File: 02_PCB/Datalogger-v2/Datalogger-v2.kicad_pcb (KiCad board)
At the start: 2 copper layers, 140 x 90 mm, 21 parts, among them U1 Micro SD Card Adapter, U7 TP4056, U8 ESP32 DEV KIT DOIT

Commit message: Update PCB layout
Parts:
- added C4: 100uF/10V, Capacitor_THT:CP_Radial_D5.0mm_P2.50mm, F.Cu at (114.5, 88.0)
- added C5: 0.1uF_0603_16V, Capacitor_SMD:C_0805_2012Metric_Pad1.18x1.45mm_HandSolder, F.Cu at (103.0, 92.0)
- added R10: 4.7Ω, Resistor_THT:R_Axial_DIN0207_L6.3mm_D2.5mm_P10.16mm_Horizontal, F.Cu at (99.0, 112.0)
- added R11: 4.7Ω, Resistor_THT:R_Axial_DIN0207_L6.3mm_D2.5mm_P10.16mm_Horizontal, F.Cu at (107.0, 112.0)
- R1, R2, R3, R4: moved to B.Cu
- moved R2 38.3 mm to (120.7, 133.7)
- moved R1 32.8 mm to (128.7, 133.7)
- moved R5 21.6 mm to (153.1, 98.0), turned to 180 degrees
- moved R7 20.7 mm to (153.2, 86.0)
- moved R6 20.7 mm to (153.2, 92.0)
- moved D1 16.6 mm to (130.1, 88.0)
- moved R4 10.2 mm to (174.4, 79.0), turned to 180 degrees
- moved R8 10.2 mm to (161.4, 121.0), turned to 180 degrees
- moved R9 10.2 mm to (161.5, 115.0), turned to 180 degrees
- moved R3 10.2 mm to (174.3, 72.0), turned to 180 degrees
- moved U6 6.00 mm to (175.7, 112.1)
- moved C2 2.96 mm to (175.0, 127.0), turned to 90 degrees
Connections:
- C1 pad 1: GND -> +5V
- C1 pad 2: +5V -> GND
- U8 pad 10: Net-(U5-SDA) -> +5V
- U8 pad 11: Net-(U5-SCL) -> +5V
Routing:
- net +5V: track 157.5 -> 336.3 mm, vias 3 -> 11
- net GND: track 149.2 -> 236.1 mm, vias 2 -> 11
- net Net-(U4-TX): track 0.00 -> 78.1 mm, vias 0 -> 4
- net Net-(U6-RX): track 0.00 -> 75.4 mm, vias 0 -> 4
- net Net-(U4-RX): track 0.00 -> 71.1 mm, vias 0 -> 2
- net +3.3V: track 103.1 -> 60.2 mm
- net Net-(U8-ADC/D4): track 0.00 -> 36.4 mm, vias 0 -> 2
- net Net-(U5-SCL): track 69.9 -> 48.9 mm, vias 1 -> 0
- net Net-(U1-MOSI): track 15.8 -> 35.2 mm, vias 0 -> 3
- net Net-(U1-CS): track 0.00 -> 19.1 mm, vias 0 -> 1
- net Net-(U1-SCK): track 0.10 -> 18.7 mm, vias 0 -> 2
- net Net-(U5-SDA): track 65.8 -> 48.7 mm, vias 1 -> 0
- net Net-(U8-ADC/DAC1/D26): track 40.6 -> 53.9 mm, vias 1 -> 2
- net Net-(U8-ADC/DAC0/D25): track 41.8 -> 55.1 mm, vias 1 -> 2
- net Net-(U2-VIN+): track 66.2 -> 56.2 mm
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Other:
- board text added: "TO DOs: - Check and change vias size - Check and change trace width (with PCB calculator in KiCad. INTERNAL LAYER result)"
- board text added: "We <3 feet here"

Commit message: Update PCB schematic
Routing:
- net GND: track 236.1 -> 295.9 mm, vias 11 -> 15
- net Net-(U8-ADC/DAC0/D25): track 55.1 -> 56.2 mm
- net +5V: vias 11 -> 10

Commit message: Update schematics and PCB design
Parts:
- moved C5 2.00 mm to (103.0, 94.0)
- moved C3 0.65 mm to (76.0, 82.0), turned to 180 degrees
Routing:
- net Net-(U8-ADC/D13): track 93.5 -> 122.8 mm
- net GND: track 295.9 -> 287.5 mm, vias 15 -> 11
- net +5V: track 336.3 -> 334.5 mm, vias 10 -> 9
- net Net-(U8-ADC/DAC0/D25): track 56.2 -> 57.6 mm, vias 2 -> 4
- net Net-(U4-RX): track 71.1 -> 72.3 mm
- net Net-(U4-TX): track 78.1 -> 78.8 mm
- net Net-(U6-RX): track 75.4 -> 75.3 mm, vias 4 -> 3
- net Net-(U5-SCL): track 48.9 -> 49.0 mm, vias 0 -> 1
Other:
- board text added: "+"
- board text added: "Gerard Way <3"
- board text added: "TO DOs: - Check and change vias size - Check and change trace width (with PCB calculator in KiCad. EXTERNAL LAYER result)"
- board text removed: "TO DOs: - Check and change vias size - Check and change trace width (with PCB calculator in KiCad. INTERNAL LAYER result)"
- board text removed: "We <3 feet here"

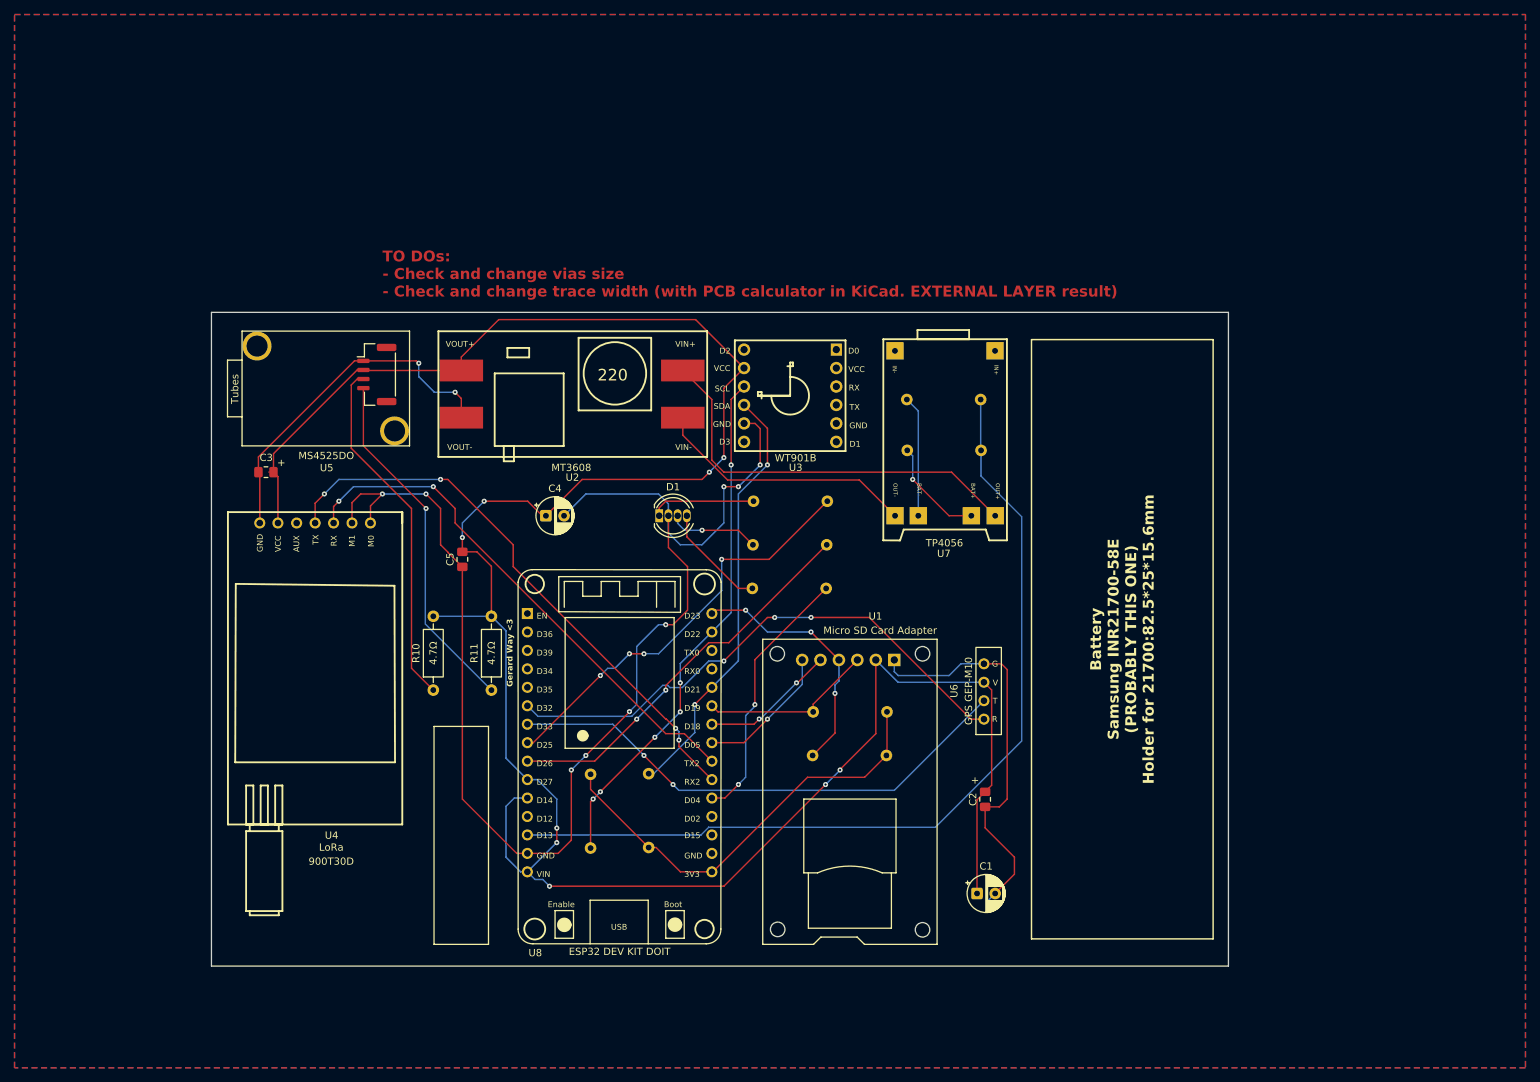
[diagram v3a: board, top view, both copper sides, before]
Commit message: Update schematic and PCB layout
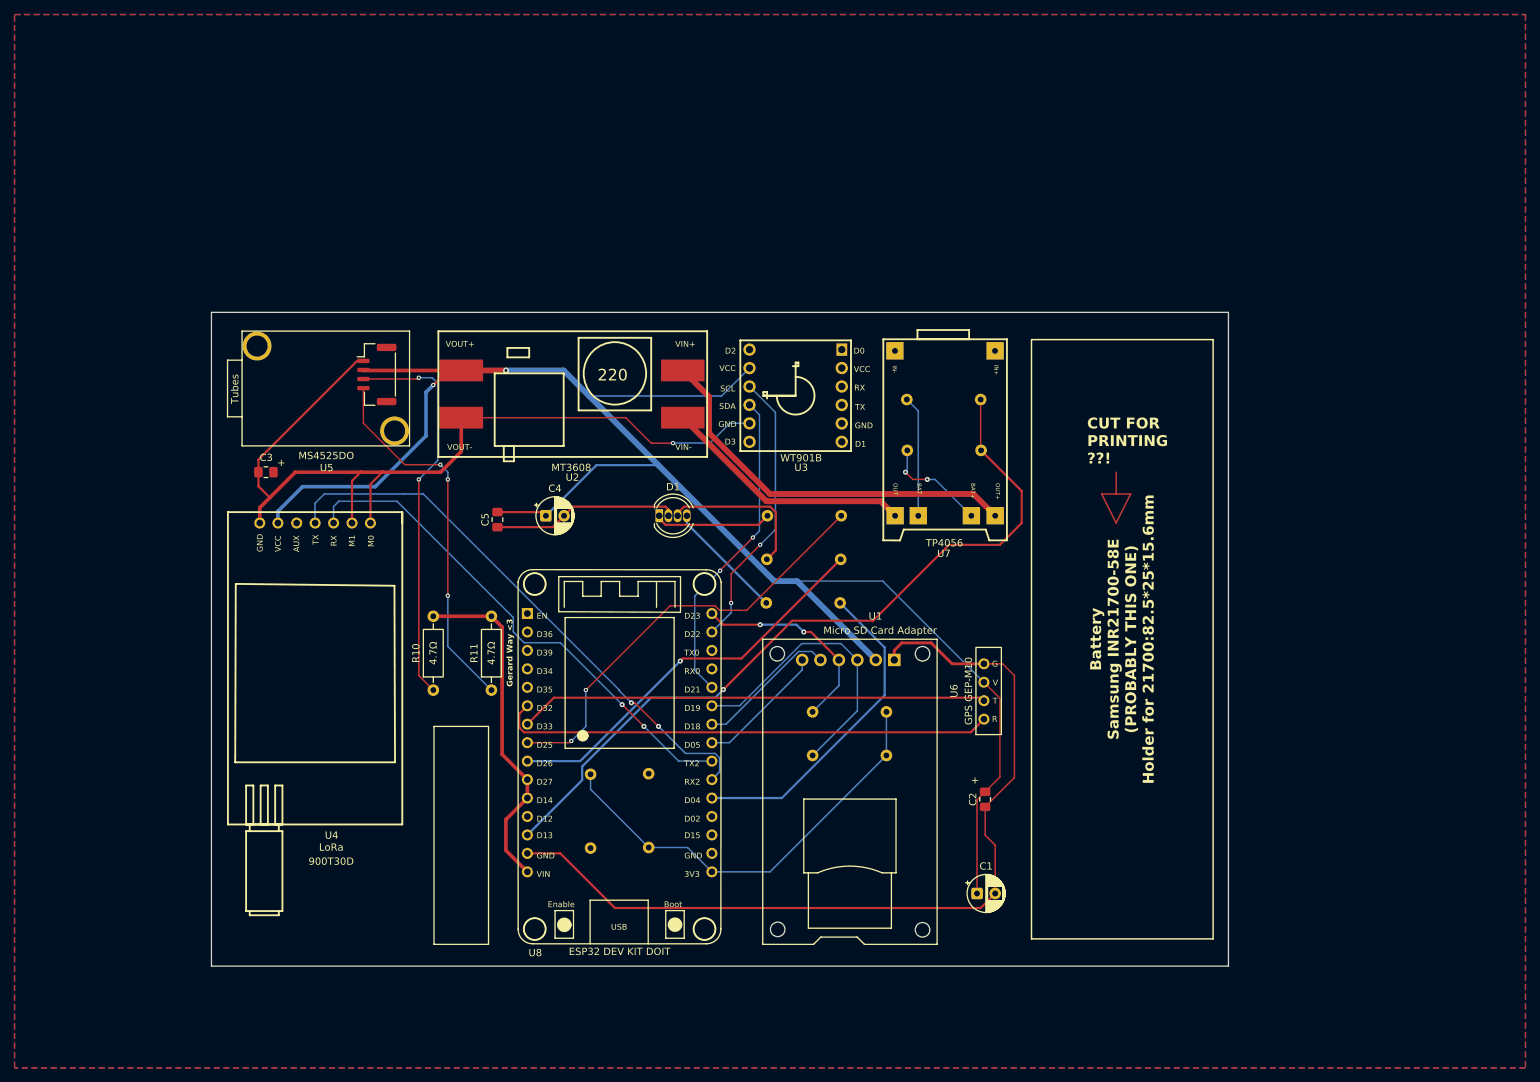
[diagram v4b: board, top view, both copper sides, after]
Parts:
- moved C5 7.29 mm to (107.8, 88.5)
- moved R9 6.00 mm to (161.4, 121.0)
- moved R8 6.00 mm to (161.4, 115.0)
- moved R6 2.77 mm to (155.1, 94.0)
- moved R5 2.77 mm to (155.0, 100.0)
- moved R7 2.77 mm to (155.2, 88.0)
- moved U3 0.75 mm to (148.8, 71.5)
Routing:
- net +5V: track 334.5 -> 284.9 mm, vias 9 -> 2
- net Net-(U3-SCL): track 72.3 -> 38.9 mm, vias 6 -> 2
- net GND: track 287.5 -> 268.2 mm, vias 11 -> 1
- net Net-(U8-ADC/D13): track 122.8 -> 106.3 mm, vias 0 -> 1
- net Net-(U1-MISO): track 24.1 -> 40.2 mm
- net Net-(U3-SDA): track 59.3 -> 44.1 mm
- net Net-(D1-VDD): track 12.6 -> 21.6 mm, vias 1 -> 0
- net Net-(U8-ADC/D4): track 36.4 -> 44.9 mm, vias 2 -> 0
- net Net-(U6-TX): track 71.7 -> 64.5 mm, vias 2 -> 0
- net Net-(U6-RX): track 75.3 -> 68.4 mm, vias 3 -> 0
- net Net-(U1-MOSI): track 35.2 -> 28.8 mm, vias 3 -> 2
- net Net-(U5-SDA): track 48.7 -> 54.8 mm, vias 0 -> 2
- net Net-(U5-SCL): track 49.0 -> 51.7 mm, vias 1 -> 3
- net Net-(U8-ADC/DAC0/D25): track 57.6 -> 59.6 mm, vias 4 -> 2
- net Net-(U2-VIN+): track 56.2 -> 54.2 mm
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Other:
- board text added: "CUT FOR PRINTING ??!"
- board text added: "Tracks width: - 5 V power: 0.8 mm - 3.3 V power: 0.2 mm - ESP32/LoRa power: 0.5 mm Via: 0.8 mm / 0.4 mm drill - SPI/UART/I2C/GPIO: 0.2 mm Via: 0.6 mm / 0.3 mm drill - Resistors/capacitors: 0.2 mm Via: 0.6 mm / 0.3 mm drill - SD Card: 0.3 mm"

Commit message: Update schematics and PCB layout
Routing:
- net Net-(U3-SCL): track 38.9 -> 80.9 mm, vias 2 -> 3
- net +5V: track 284.9 -> 317.9 mm, vias 2 -> 3
- net Net-(U3-SDA): track 44.1 -> 60.1 mm
- net Net-(BT1-+): track 14.7 -> 27.2 mm, vias 2 -> 0
- net Net-(U6-TX): track 64.5 -> 66.6 mm
- net Net-(U5-SDA): track 54.8 -> 53.3 mm
- net GND: track 268.2 -> 268.8 mm
- net Net-(U6-RX): track 68.4 -> 68.6 mm, vias 0 -> 2
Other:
- outline, holes or cut-outs redrawn
- board text added: "CHECK DIMENSIONS OF CUT"
- board text added: "Important for soldering and assembling"
- board text added: "Tracks width: - 5 V power: 0.8 mm - 3.3 V power: 0.2 mm - ESP32/LoRa power: 0.5 mm - SPI/UART/I2C/GPIO: 0.2 mm - Resistors/capacitors: 0.2 mm - SD Card: 0.3 mm Vias: 0.7 mm / 0.3 mm drill"
- board text removed: "CUT FOR PRINTING ??!"
- board text removed: "Logo of Aisler will go here c: (remove this ^ comment before submitting lol)"
- board text removed: "TO DOs: - Check and change vias size - Check and change trace width (with PCB calculator in KiCad. EXTERNAL LAYER result)"
- board text removed: "Tracks width: - 5 V power: 0.8 mm - 3.3 V power: 0.2 mm - ESP32/LoRa power: 0.5 mm Via: 0.8 mm / 0.4 mm drill - SPI/UART/I2C/GPIO: 0.2 mm Via: 0.6 mm / 0.3 mm drill - Resistors/capacitors: 0.2 mm Via: 0.6 mm / 0.3 mm drill - SD Card: 0.3 mm"

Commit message: Update PCB layout
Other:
- board size 140 x 90 mm -> 112.9 x 90 mm
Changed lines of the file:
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@@
 	(title_block
 		(title "Flight Logger NFC 2027")
-		(date "2026-08-03")
+		(date "2026-08-10")
 		(company "Neues Fliegen e.V.")
 		(comment 1 "Mirella Borean")
@@
 			(outputformat 1)
 			(mirror no)
-			(drillshape 1)
+			(drillshape 0)
 			(scaleselection 1)
-			(outputdirectory "")
+			(outputdirectory "../Gerbers/")
 		)
 	)
@@
 		(end 99.1 147)
 		(stroke
-			(width 0.1)
-			(type default)
+			(width 0.08382)
+			(type solid)
 		)
 		(layer "F.SilkS")
@@
 		(end 106.6 147)
 		(stroke
-			(width 0.1)
-			(type default)
+			(width 0.08382)
+			(type solid)
 		)
 		(layer "F.SilkS")
@@
 		(end 99.1 117)
 		(stroke
-			(width 0.1)
-			(type default)
+			(width 0.08382)
+			(type solid)
 		)
 		(layer "F.SilkS")
@@
 		(end 106.6 117)
 		(stroke
-			(width 0.1)
-			(type default)
+			(width 0.08382)
+			(type solid)
 		)
 		(layer "F.SilkS")
@@
 	)
 	(gr_rect
-		(start 68.4601 60)
-		(end 208.4601 150)
+		(start 181.35 63.75)
+		(end 206.35 146.25)
 		(stroke
-			(width 0.05)
+			(width 0.2)
 			(type solid)
 		)
 		(fill no)
-		(layer "Edge.Cuts")
+		(layer "Cmts.User")
 	)
 	(gr_rect
-		(start 181.35 63.75)
-		(end 206.35 146.25)
+		(start 68.4601 60)
+		(end 181.35 150)
 		(stroke
-			(width 0.2)
+			(width 0.05)
 			(type solid)
 		)
@@
 				)
 			)
+		)
+	)
+	(dimension
+		(type orthogonal)
+		(layer "Cmts.User")
+		(pts
+			(xy 68.4601 60) (xy 181.35 60)
+		)
+		(height -5)
+		(orientation 0)
+		(format
+			(prefix "")
+			(suffix "")
+			(units 3)
+			(units_format 0)
+			(precision 4)
+			(suppress_zeroes yes)
+		)
+		(style
+			(thickness 0.1)
+			(arrow_length 1.27)
+			(text_position_mode 0)
+			(arrow_direction outward)
+			(extension_height 0.58642)
+			(extension_offset 0.5)
+			(keep_text_aligned yes)
+		)
+		(gr_text "112.8899"
+			(at 124.90505 53.9 0)
+			(layer "Cmts.User")
+			(effects
+				(font
+					(size 1 1)
+					(thickness 0.1)
+				)
+			)
